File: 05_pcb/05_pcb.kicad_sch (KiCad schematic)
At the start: 14 parts, among them J1 MPU6050, J2 USB_C_Receptacle_USB2.0_16P, U1 ATmega328P-A, U2 W25Q128JVS, U3 CH340C, U4 MCP73831-2-OT, U5 MCP1700x-330xxTT

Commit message: Schematic and PCB update
Development of the pcb
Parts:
- added C4, C5, C6: 100n, Capacitor_SMD:C_0805_2012Metric, symbol Device:C
- added R3, R4: 5.1k, Resistor_SMD:R_0805_2012Metric, symbol Device:R_US
- added R5, R6: 1k, Resistor_SMD:R_0805_2012Metric, symbol Device:R_US
- added R7, R8: 10k, Resistor_SMD:R_0805_2012Metric, symbol Device:R_US
- added SW1: SW_Nidec_CAS-120A1, Button_Switch_SMD:Nidec_Copal_CAS-120A, symbol Switch:SW_Nidec_CAS-120A1
- BT1: footprint (none) -> Battery:BatteryHolder_MYOUNG_BS-07-A1BJ001_CR2032
- C1, C2, C3: footprint (none) -> Capacitor_SMD:C_0805_2012Metric
- D1: footprint (none) -> LED_SMD:LED_0805_2012Metric
- J1: footprint (none) -> Connector_PinSocket_2.54mm:PinSocket_1x08_P2.54mm_Vertical
- J2: footprint (none) -> Connector_USB:USB_C_Receptacle_Amphenol_124019772112A
- R1, R2: footprint (none) -> Resistor_SMD:R_0805_2012Metric
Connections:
- net +3.3V: now also U2.3 (~{WP}/IO_{2}), U2.7 (~{HOLD}/~{RESET}/IO_{3}); no longer C3.1, J1.VCC (Pin_1), U1.4 (VCC), U1.6 (VCC), U2.8 (VCC), U5.2 (VO)
- net GND: now also J1.2 (Pin_2), J1.7 (Pin_7), C4.2, C6.1, R3.2, R4.2; no longer J1.GND (Pin_2)
- net Vbat: now also SW1.2 (B); no longer C2.1, U5.3 (VI)
- net at J2.A5 (CC1): now also R4.1
- net D+: now reaches J2.A6 (D+)
- net D+: now also J2.B6 (D+), U3.5 (UD+)
- net D-: now reaches J2.A7 (D-)
- net D-: now also J2.B7 (D-), U3.6 (UD-)
- net at J2.B5 (CC2): now also R3.1
- net CS: now reaches U1.14 (PB2)
- net CS: now also U2.1 (~{CS}), R8.1
- net MOSI: now reaches U1.15 (PB3)
- net MOSI: now also U2.5 (DI/IO_{0})
- net MISO: now reaches U1.16 (PB4)
- net MISO: now also U2.2 (DO/IO_{1})
- net CLK: now reaches U1.17 (PB5)
- net CLK: now also U2.6 (CLK)
- net SDA: now reaches U1.27 (PC4)
- net SDA: now also J1.4 (Pin_4)
- net SCL: now reaches U1.28 (PC5)
- net SCL: now also J1.3 (Pin_3)
- net RST: now reaches U1.29 (~{RESET}/PC6)
- net RST: now also C5.1, R7.2
- net RX: now reaches U1.30 (PD0)
- net RX: now also R5.2
- net TX: now reaches U1.31 (PD1)
- net TX: now also R6.2
- net INT: now reaches U1.32 (PD2)
- net INT: now also J1.8 (Pin_8)
- net at U3.13 (~{DTR}): now also C5.2
- net at U3.2 (TXD): now also R5.1
- net at U3.3 (RXD): now also R6.1
- net at U3.4 (V3): now also C4.1
- net +5V renamed Vbus
- new net: C2.1, SW1.3 (A), U5.3 (VI)
- new net Vcc: C3.1, C6.2, J1.1 (Pin_1), R7.1, R8.2, U1.4 (VCC), U1.6 (VCC), U2.8 (VCC), U5.2 (VO)
- no-connect marks 0 -> 28
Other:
- moved on the sheet: C1, D1, R1, R2, U4

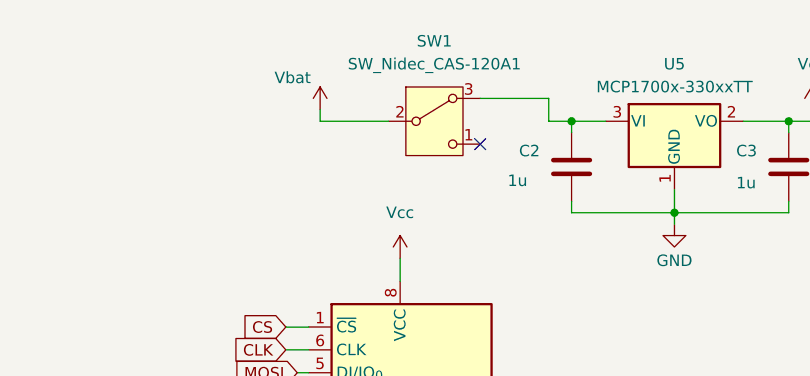
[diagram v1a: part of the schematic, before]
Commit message: New switch footprint and USBC connector
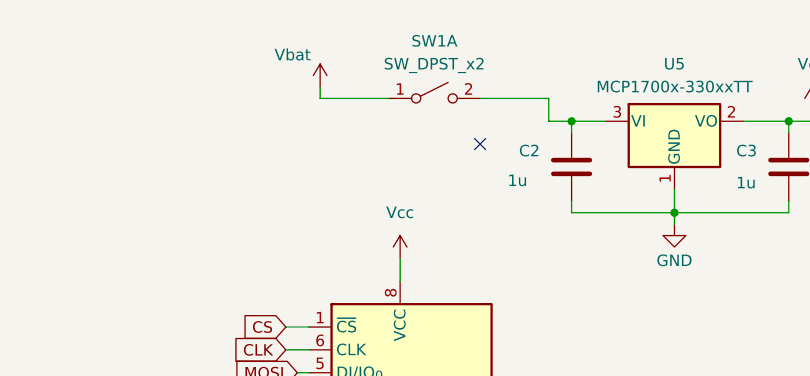
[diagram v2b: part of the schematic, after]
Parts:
- removed SW1: SW_Nidec_CAS-120A1, Button_Switch_SMD:Nidec_Copal_CAS-120A, symbol Switch:SW_Nidec_CAS-120A1
- added SW1: SW_DPST_x2, Button_Switch_THT:SW_DIP_SPSTx01_Slide_6.7x4.1mm_W7.62mm_P2.54mm_LowProfile, symbol Switch:SW_DPST_x2
- J2: footprint Connector_USB:USB_C_Receptacle_Amphenol_124019772112A -> Connector_USB:USB_C_Receptacle_HCTL_HC-TYPE-C-16P-01A
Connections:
- net Vbat: now also SW1.1 (A)
- net at C2.1, U5.3 (VI): now also SW1.2 (B)
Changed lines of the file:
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@@
 	(wire
 		(pts
-			(xy 95.25 29.21) (xy 95.25 30.48)
+			(xy 95.25 26.67) (xy 95.25 27.94)
 		)
 		(stroke
@@
 	(wire
 		(pts
-			(xy 95.25 30.48) (xy 102.87 30.48)
+			(xy 95.25 27.94) (xy 102.87 27.94)
 		)
 		(stroke
@@
 			)
 		)
-		(property "Footprint" "Connector_USB:USB_C_Receptacle_Amphenol_124019772112A"
+		(property "Footprint" "Connector_USB:USB_C_Receptacle_HCTL_HC-TYPE-C-16P-01A"
 			(at 36.83 81.28 0)
 			(effects
@@
 	(symbol
 		(lib_id "power:VCC")
-		(at 95.25 29.21 0)
+		(at 95.25 26.67 0)
 		(unit 1)
 		(exclude_from_sim no)
@@
 		(dnp no)
 		(property "Reference" "#PWR016"
-			(at 95.25 33.02 0)
+			(at 95.25 30.48 0)
 			(effects
 				(font
@@
 		)
 		(property "Value" "Vbat"
-			(at 92.202 25.654 0)
+			(at 92.202 23.114 0)
 			(effects
 				(font
@@
 		)
 		(property "Footprint" ""
-			(at 95.25 29.21 0)
+			(at 95.25 26.67 0)
 			(effects
 				(font
@@
 		)
 		(property "Datasheet" ""
-			(at 95.25 29.21 0)
+			(at 95.25 26.67 0)
 			(effects
 				(font
@@
 		)
 		(property "Description" "Power symbol creates a global label with name \"VCC\""
-			(at 95.25 29.21 0)
+			(at 95.25 26.67 0)
 			(effects
 				(font
@@
 	)
 	(symbol
-		(lib_id "Switch:SW_Nidec_CAS-120A1")
-		(at 107.95 30.48 0)
-		(unit 1)
-		(exclude_from_sim no)
-		(in_bom yes)
-		(on_board yes)
-		(dnp no)
-		(fields_autoplaced yes)
-		(property "Reference" "SW1"
-			(at 107.95 21.59 0)
-			(effects
-				(font
-					(size 1.27 1.27)
-				)
-			)
-		)
-		(property "Value" "SW_Nidec_CAS-120A1"
-			(at 107.95 24.13 0)
-			(effects
-				(font
-					(size 1.27 1.27)
-				)
-			)
-		)
-		(property "Footprint" "Button_Switch_SMD:Nidec_Copal_CAS-120A"
-			(at 107.95 40.64 0)
-			(effects
-				(font
-					(size 1.27 1.27)
-				)
-				(hide yes)
-			)
-		)
-		(property "Datasheet" "https://www.nidec-components.com/e/catalog/switch/cas.pdf"
-			(at 107.95 38.1 0)
-			(effects
-				(font
-					(size 1.27 1.27)
-				)
-				(hide yes)
-			)
-		)
-		(property "Description" "Switch, single pole double throw"
-			(at 107.95 30.48 0)
-			(effects
-				(font
-					(size 1.27 1.27)
-				)
-				(hide yes)
-			)
-		)
-		(pin "3"
-		)
-		(pin "1"
-		)
-		(pin "2"
-		)
-		(instances
-			(project ""
-				(path "/19acda86-b56a-42f1-8399-2bfa01fb868e"
-					(reference "SW1")
-					(unit 1)
-				)
-			)
-		)
-	)
-	(symbol
 		(lib_id "Device:C")
 		(at 201.93 34.29 0)
@@
 					(unit 1)
 				)
+			)
+		)
+	)
+	(symbol
+		(lib_id "Switch:SW_DPST_x2")
+		(at 107.95 27.94 0)
+		(unit 1)
+		(exclude_from_sim no)
+		(in_bom yes)
+		(on_board yes)
+		(dnp no)
+		(fields_autoplaced yes)
+		(property "Reference" "SW1"
+			(at 107.95 21.59 0)
+			(effects
+				(font
+					(size 1.27 1.27)
+				)
+			)
+		)
+		(property "Value" "SW_DPST_x2"
+			(at 107.95 24.13 0)
+			(effects
+				(font
+					(size 1.27 1.27)
+				)
+			)
+		)
+		(property "Footprint" "Button_Switch_THT:SW_DIP_SPSTx01_Slide_6.7x4.1mm_W7.62mm_P2.54mm_LowProfile"
+			(at 107.95 27.94 0)
+			(effects
+				(font
+					(size 1.27 1.27)
+				)
+				(hide yes)
+			)
+		)
+		(property "Datasheet" "~"
+			(at 107.95 27.94 0)
+			(effects
+				(font
+					(size 1.27 1.27)
+				)
+				(hide yes)
+			)
+		)
+		(property "Description" "Single Pole Single Throw (SPST) switch, separate symbol"
+			(at 107.95 27.94 0)
+			(effects
+				(font
+					(size 1.27 1.27)
+				)
+				(hide yes)
+			)
+		)
+		(pin "1"
+		)
+		(pin "2"
+		)
+		(pin "4"
+		)
+		(pin "3"
+		)
+		(instances
+			(project ""
+				(path "/19acda86-b56a-42f1-8399-2bfa01fb868e"
+					(reference "SW1")
+					(unit 1)
+				)
